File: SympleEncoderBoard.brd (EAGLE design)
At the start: 50.8 x 50.8 mm, 31 parts, among them IC1 STM32F446RET6

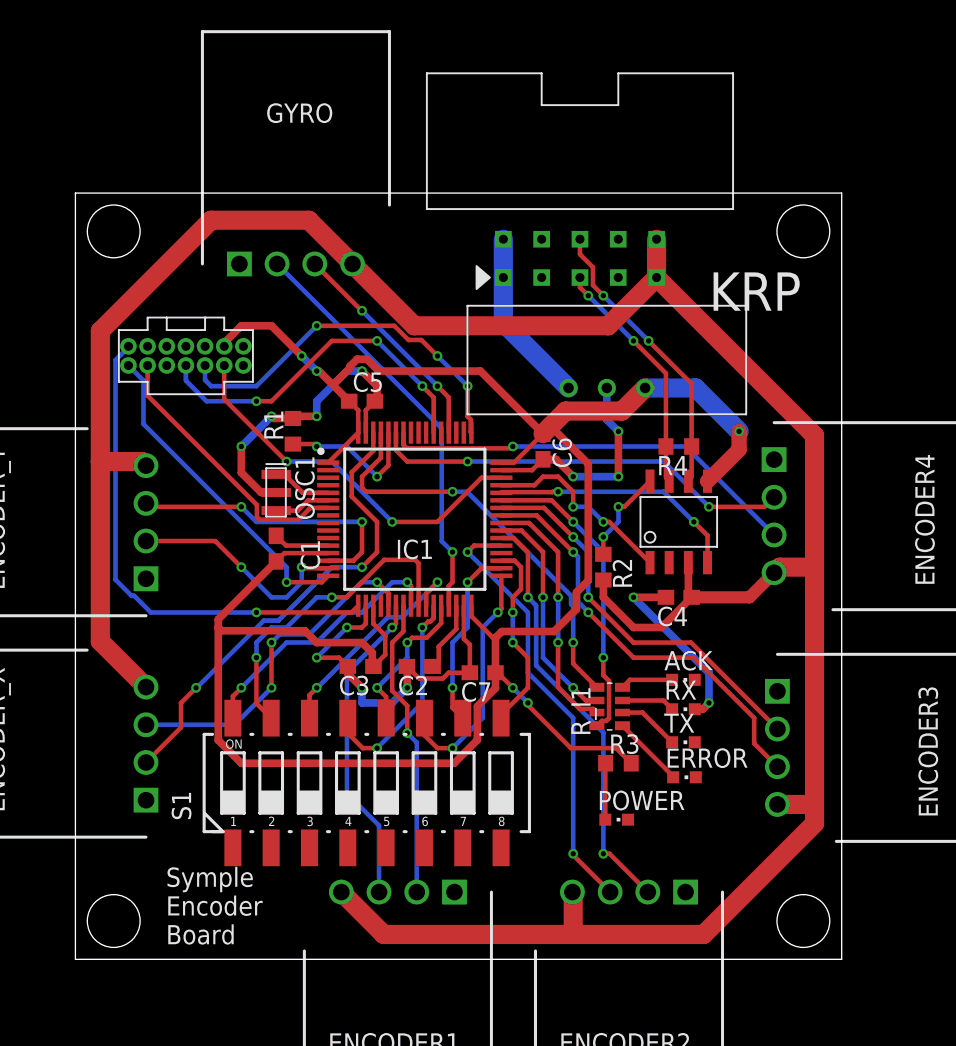
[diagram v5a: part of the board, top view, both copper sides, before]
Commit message: GYRO用XHコネクタを横から縦に、テキストの文字を少し拡大、ベタパターンDRCチェック済
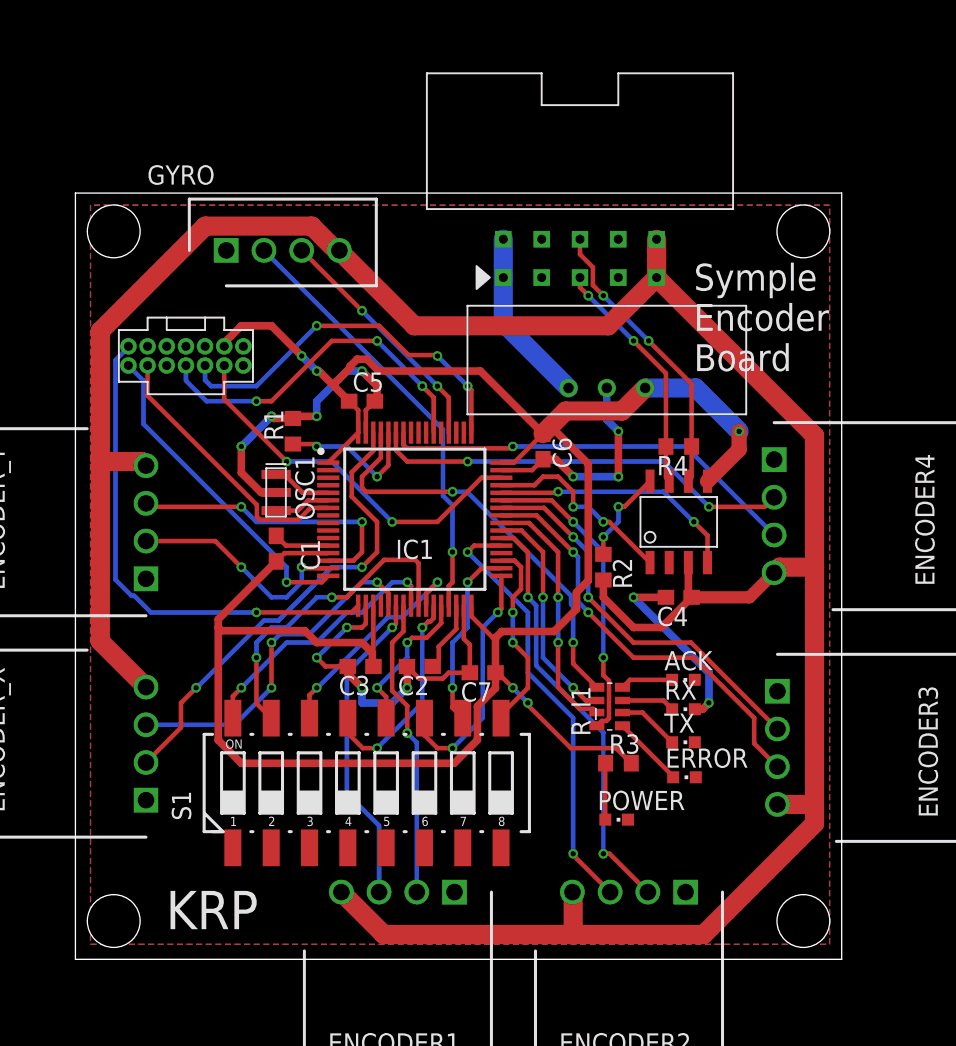
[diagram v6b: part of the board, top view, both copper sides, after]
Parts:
- GYRO: value S4B-XH-A_LF__SN_ -> B4B-XH-A_LF__SN_; device S4B-XH-A_LF__SN_:SHDRRA4W64P0X250_1X4_1240X1150 -> B4B-XH-A_LF__SN_:SHDR4W64P0X250_1X4_1240X575X70
- moved GYRO 1.25 mm to (10.0, 47.0)
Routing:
- net I2C_SCL: track 27.6 -> 28.8 mm
- net I2C_SDA: track 14.9 -> 16.1 mm
- net +3.3V: track 149.6 -> 149.0 mm
- added copper zone on layer 1, net GND
- added copper zone on layer 16, net GND

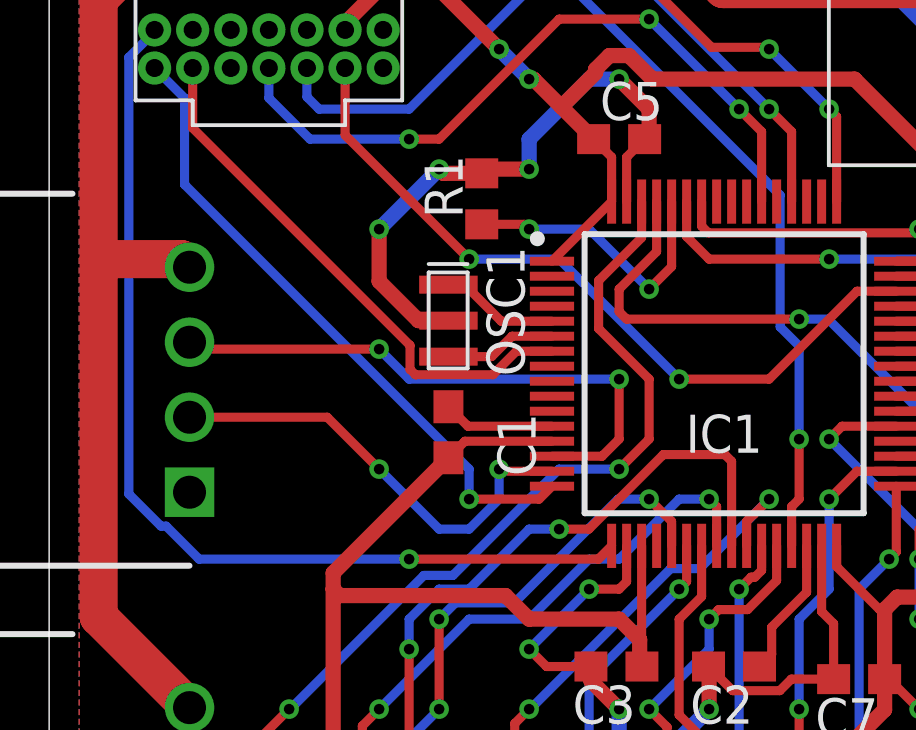
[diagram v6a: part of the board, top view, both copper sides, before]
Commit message: GRYO用コネクタを横から縦に、テキストの文字を少し拡大、ベタパターンDRCチェック済、ガーバーデータ追加
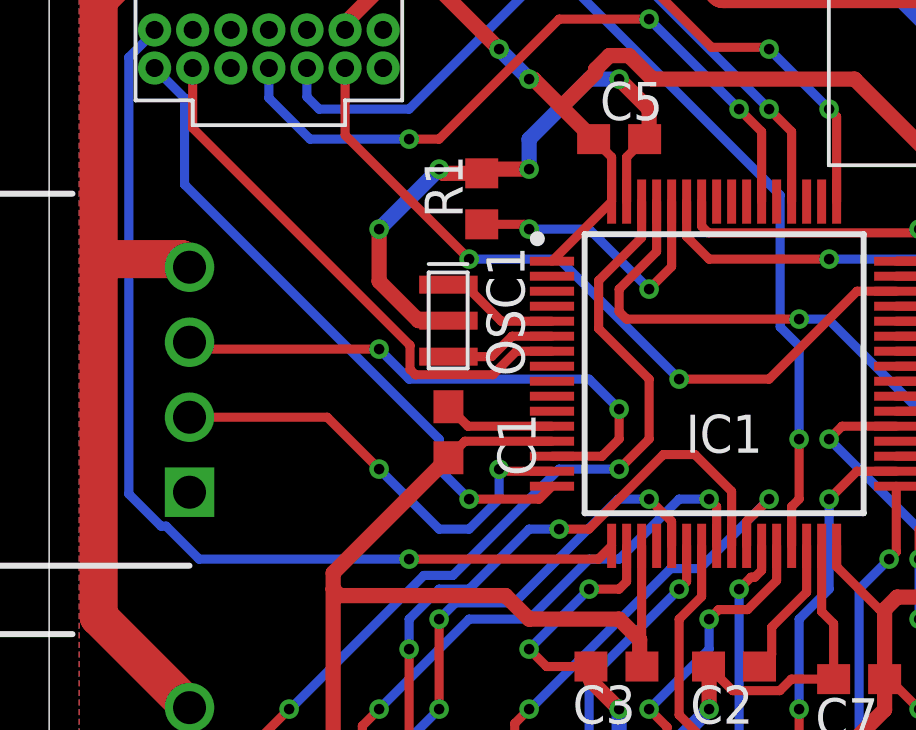
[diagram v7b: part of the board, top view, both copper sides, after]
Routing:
- net SW7: track 21.3 -> 20.8 mm
- net ENY_A: track 19.3 -> 18.7 mm
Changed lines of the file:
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@@
 <wire x1="16.332" y1="25" x2="14" y2="25" width="0.3048" layer="1"/>
 <via x="14" y="25" extent="1-16" drill="0.35"/>
-<wire x1="14" y1="25" x2="14" y2="26" width="0.3048" layer="16"/>
-<wire x1="14" y1="26" x2="4.515" y2="35.485" width="0.3048" layer="16"/>
+<wire x1="13" y1="27" x2="13" y2="26" width="0.3048" layer="16"/>
+<wire x1="14" y1="25" x2="13" y2="26" width="0.3048" layer="16"/>
+<wire x1="13" y1="27" x2="4.515" y2="35.485" width="0.3048" layer="16"/>
 <wire x1="4.515" y1="38.37" x2="4.515" y2="35.485" width="0.3048" layer="16"/>
 <wire x1="4.515" y1="38.37" x2="3.515" y2="39.37" width="0.3048" layer="16"/>
@@
 <contactref element="IC1" pad="14"/>
 <contactref element="ENCODER_Y" pad="3"/>
-<via x="19" y="29" extent="1-16" drill="0.35"/>
-<wire x1="19" y1="29" x2="12" y2="29" width="0.3048" layer="16"/>
+<via x="19" y="28" extent="1-16" drill="0.35"/>
+<wire x1="19" y1="28" x2="18" y2="29" width="0.3048" layer="16"/>
+<wire x1="18" y1="29" x2="12" y2="29" width="0.3048" layer="16"/>
 <wire x1="12" y1="29" x2="11" y2="30" width="0.3048" layer="16"/>
 <via x="11" y="30" extent="1-16" drill="0.35"/>
 <wire x1="11" y1="30" x2="4.91" y2="30" width="0.3048" layer="1"/>
 <wire x1="4.91" y1="30" x2="4.68" y2="30.23" width="0.3048" layer="1"/>
-<wire x1="19" y1="29" x2="19" y2="27" width="0.3048" layer="1"/>
+<wire x1="19" y1="28" x2="19" y2="27" width="0.3048" layer="1"/>
 <wire x1="19" y1="27" x2="18.43" y2="26.43" width="0.3048" layer="1"/>
 <wire x1="18.43" y1="26.43" x2="16.762" y2="26.43" width="0.3048" layer="1"/>
@@
 <wire x1="17" y1="24" x2="17.98945" y2="24" width="0.3048" layer="1"/>
 <wire x1="20.47375" y1="26.4843" x2="17.98945" y2="24" width="0.3048" layer="1"/>
-<wire x1="22.52625" y1="26.4843" x2="20.47375" y2="26.4843" width="0.3048" layer="1"/>
+<wire x1="21.52625" y1="26.4843" x2="20.47375" y2="26.4843" width="0.3048" layer="1"/>
 <wire x1="12.98" y1="15.99" x2="12" y2="16.97" width="0.3048" layer="1"/>
 <wire x1="12" y1="16.97" x2="12" y2="20" width="0.3048" layer="1"/>
@@
 <via x="12" y="20" extent="1-16" drill="0.35"/>
 <wire x1="17" y1="24" x2="16" y2="24" width="0.3048" layer="16"/>
-<wire x1="22.75" y1="23.442" x2="22.75" y2="26.26055" width="0.3048" layer="1"/>
-<wire x1="22.75" y1="26.26055" x2="22.52625" y2="26.4843" width="0.3048" layer="1"/>
+<wire x1="22.75" y1="23.442" x2="22.75" y2="25.26055" width="0.3048" layer="1"/>
+<wire x1="22.75" y1="25.26055" x2="21.52625" y2="26.4843" width="0.3048" layer="1"/>
 <wire x1="16" y1="24" x2="14" y2="22" width="0.3048" layer="16"/>
 <wire x1="14" y1="22" x2="13" y2="22" width="0.3048" layer="16"/>

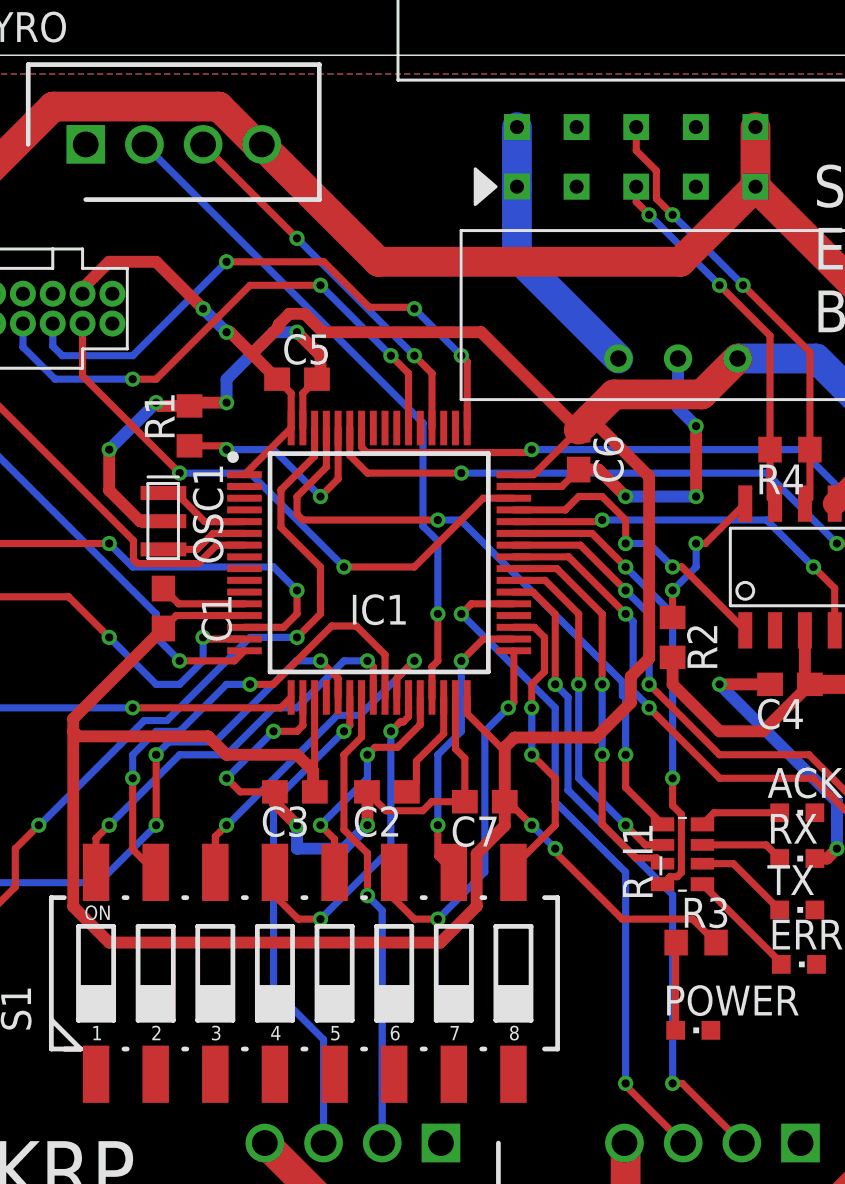
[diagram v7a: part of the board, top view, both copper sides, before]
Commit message: 配線を何箇所か短くした
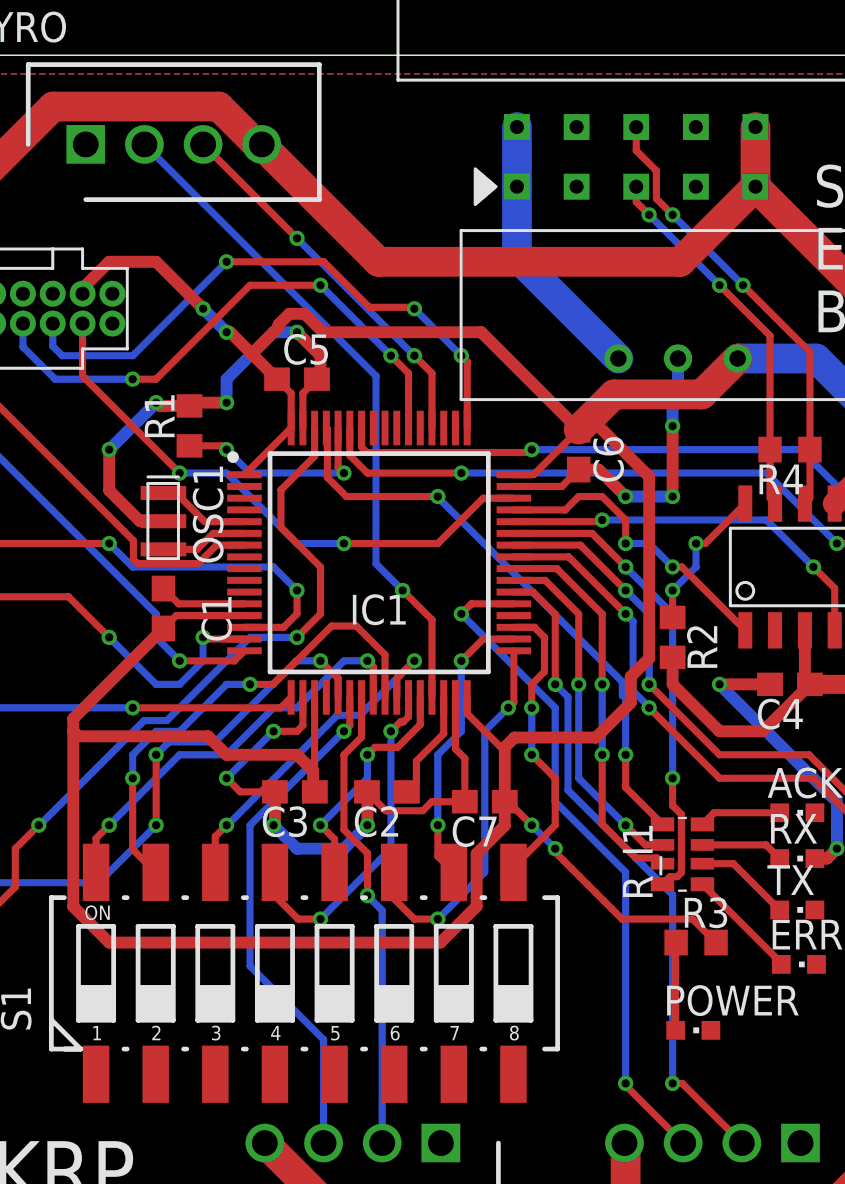
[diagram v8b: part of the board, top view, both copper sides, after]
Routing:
- net LEDGYRO: track 27.8 -> 25.1 mm
- net GND: track 75.6 -> 74.4 mm
- net SWDIO: track 25.2 -> 24.4 mm
- net EN1_A: track 21.2 -> 22.0 mm
- net N$1: track 9.70 -> 9.08 mm
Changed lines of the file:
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@@
 <wire x1="26.15" y1="20.85" x2="26.15" y2="19" width="0.3048" layer="1"/>
 <wire x1="25.75" y1="21.25" x2="26.15" y2="20.85" width="0.3048" layer="1"/>
-<wire x1="18.06" y1="19.42" x2="18.06" y2="18.94" width="0.508" layer="1"/>
-<wire x1="18.06" y1="18.94" x2="19" y2="18" width="0.508" layer="1"/>
+<wire x1="18.06" y1="19.42" x2="18.06" y2="18.06" width="0.508" layer="1"/>
+<wire x1="18.06" y1="18.06" x2="18" y2="18" width="0.508" layer="1"/>
 <wire x1="21.98" y1="19.42" x2="22" y2="19.4" width="0.508" layer="1"/>
 <wire x1="22" y1="19.4" x2="22" y2="18" width="0.508" layer="1"/>
-<via x="19" y="18" extent="1-16" drill="0.35"/>
+<via x="18" y="18" extent="1-16" drill="0.35"/>
 <via x="22" y="18" extent="1-16" drill="0.35"/>
-<wire x1="19" y1="18" x2="19" y2="17" width="0.508" layer="16"/>
+<wire x1="18" y1="18" x2="19" y2="17" width="0.508" layer="16"/>
 <wire x1="21" y1="17" x2="19" y2="17" width="0.508" layer="16"/>
 <wire x1="21" y1="17" x2="22" y2="18" width="0.508" layer="16"/>
@@
 <wire x1="31.85" y1="33.15" x2="33" y2="32" width="0.508" layer="1"/>
 <via x="33" y="32" extent="1-16" drill="0.35"/>
-<wire x1="33" y1="32" x2="36" y2="32" width="0.508" layer="16"/>
-<wire x1="35.23" y1="37.88" x2="35.23" y2="35.77" width="0.508" layer="16"/>
-<wire x1="35.23" y1="35.77" x2="36" y2="35" width="0.508" layer="16"/>
-<via x="36" y="35" extent="1-16" drill="0.35"/>
-<via x="36" y="32" extent="1-16" drill="0.35"/>
-<wire x1="36" y1="35" x2="36" y2="32" width="0.508" layer="1"/>
+<wire x1="33" y1="32" x2="35" y2="32" width="0.508" layer="16"/>
+<wire x1="35.23" y1="37.88" x2="35.23" y2="36.23" width="0.508" layer="16"/>
+<wire x1="35.23" y1="36.23" x2="35" y2="36" width="0.508" layer="16"/>
+<wire x1="35" y1="36" x2="35" y2="35" width="0.508" layer="16"/>
+<via x="35" y="35" extent="1-16" drill="0.35"/>
+<via x="35" y="32" extent="1-16" drill="0.35"/>
+<wire x1="35" y1="35" x2="35" y2="32" width="0.508" layer="1"/>
 <wire x1="24.74105" y1="19" x2="26.15" y2="19" width="0.3048" layer="1"/>
 <wire x1="24.35625" y1="18.6152" x2="24.74105" y2="19" width="0.3048" layer="1"/>
@@
 <wire x1="34.57" y1="18.035" x2="33" y2="19.605" width="0.3048" layer="1"/>
 <wire x1="33" y1="19.605" x2="33" y2="21" width="0.3048" layer="1"/>
-<wire x1="20.25" y1="34.918" x2="20.25" y2="33.25" width="0.3048" layer="1"/>
-<wire x1="20.25" y1="33.25" x2="19" y2="32" width="0.3048" layer="1"/>
-<wire x1="19" y1="32" x2="19" y2="31.25" width="0.3048" layer="1"/>
-<wire x1="19" y1="31.25" x2="19.25" y2="31" width="0.3048" layer="1"/>
-<wire x1="25" y1="31" x2="25.9659125" y2="31" width="0.3048" layer="16"/>
-<via x="25" y="31" extent="1-16" drill="0.35"/>
-<wire x1="19.25" y1="31" x2="25" y2="31" width="0.3048" layer="1"/>
+<wire x1="25" y1="32" x2="24.98295625" y2="31.98295625" width="0.3048" layer="16"/>
+<via x="25" y="32" extent="1-16" drill="0.35"/>
 <wire x1="32.8598" y1="24.1061125" x2="32.8598" y2="23.52770625" width="0.3048" layer="16"/>
 <wire x1="32.8598" y1="23.52770625" x2="33" y2="23.38750625" width="0.3048" layer="16"/>
 <wire x1="33" y1="23.38750625" x2="33" y2="21" width="0.3048" layer="16"/>
-<wire x1="25.9659125" y1="31" x2="32.8598" y2="24.1061125" width="0.3048" layer="16"/>
+<wire x1="24.98295625" y1="31.98295625" x2="32.8598" y2="24.1061125" width="0.3048" layer="16"/>
+<wire x1="20.25" y1="34.918" x2="20.2928" y2="34.8752" width="0.3048" layer="1"/>
+<wire x1="20.2928" y1="34.8752" x2="20.2928" y2="32.81313125" width="0.3048" layer="1"/>
+<wire x1="20.2928" y1="32.81313125" x2="21.10593125" y2="32" width="0.3048" layer="1"/>
+<wire x1="21.10593125" y1="32" x2="25" y2="32" width="0.3048" layer="1"/>
 </signal>
 <signal name="N$1">
 <contactref element="R1" pad="1"/>
 <contactref element="IC1" pad="60"/>
-<wire x1="20.75" y1="34.918" x2="20.75" y2="32.75" width="0.3048" layer="1"/>
-<wire x1="20.75" y1="32.75" x2="20" y2="32" width="0.3048" layer="1"/>
+<wire x1="20.75" y1="34.918" x2="20.75" y2="33.249996875" width="0.3048" layer="1"/>
+<wire x1="20.75" y1="33.249996875" x2="21" y2="33" width="0.3048" layer="1"/>
 <via x="16" y="34" extent="1-16" drill="0.35"/>
-<via x="20" y="32" extent="1-16" drill="0.35"/>
-<wire x1="20" y1="32" x2="18" y2="34" width="0.3048" layer="16"/>
-<wire x1="18" y1="34" x2="16" y2="34" width="0.3048" layer="16"/>
+<via x="21" y="33" extent="1-16" drill="0.35"/>
+<wire x1="21" y1="33" x2="17" y2="33" width="0.3048" layer="16"/>
+<wire x1="17" y1="33" x2="16" y2="34" width="0.3048" layer="16"/>
 <wire x1="14.42" y1="34.16" x2="15.84" y2="34.16" width="0.3048" layer="1"/>
 <wire x1="15.84" y1="34.16" x2="16" y2="34" width="0.3048" layer="1"/>
@@
 <contactref element="IC1" pad="46"/>
 <contactref element="U$1" pad="4"/>
-<via x="21" y="29" extent="1-16" drill="0.35"/>
+<via x="21" y="30" extent="1-16" drill="0.35"/>
 <via x="14" y="33" extent="1-16" drill="0.35"/>
-<wire x1="14" y1="33" x2="17" y2="33" width="0.3048" layer="16"/>
-<wire x1="21" y1="29" x2="17" y2="33" width="0.3048" layer="16"/>
+<wire x1="14" y1="33" x2="16" y2="33" width="0.3048" layer="16"/>
+<wire x1="21" y1="30" x2="19" y2="30" width="0.3048" layer="16"/>
+<wire x1="19" y1="30" x2="16" y2="33" width="0.3048" layer="16"/>
 <wire x1="14" y1="33" x2="9.865" y2="37.135" width="0.3048" layer="1"/>
 <wire x1="9.865" y1="37.135" x2="9.865" y2="39.37" width="0.3048" layer="1"/>
-<wire x1="26.93" y1="31.93" x2="24" y2="29" width="0.3048" layer="1"/>
-<wire x1="21" y1="29" x2="24" y2="29" width="0.3048" layer="1"/>
+<wire x1="26.93" y1="31.93" x2="25" y2="30" width="0.3048" layer="1"/>
+<wire x1="25" y1="30" x2="21" y2="30" width="0.3048" layer="1"/>
 <wire x1="28.238" y1="31.93" x2="26.93" y2="31.93" width="0.3048" layer="1"/>
 </signal>
@@
 <signal name="I2C_SCL">
 <contactref element="IC1" pad="29"/>
-<wire x1="24.75" y1="23.442" x2="24.75" y2="24.75" width="0.3048" layer="1"/>
-<wire x1="24.75" y1="24.75" x2="25" y2="25" width="0.3048" layer="1"/>
-<wire x1="25" y1="25" x2="25" y2="27" width="0.3048" layer="1"/>
-<via x="25" y="27" extent="1-16" drill="0.35"/>
+<wire x1="24.75" y1="26.75" x2="24.75" y2="23.442" width="0.3048" layer="1"/>
+<wire x1="24.75" y1="26.75" x2="23.5" y2="28" width="0.3048" layer="1"/>
+<via x="23.5" y="28" extent="1-16" drill="0.35"/>
 <contactref element="GYRO" pad="2"/>
-<wire x1="25" y1="30.10593125" x2="25" y2="27" width="0.3048" layer="16"/>
-<wire x1="24.3678" y1="30.73813125" x2="25" y2="30.10593125" width="0.3048" layer="16"/>
-<wire x1="12.5" y1="47" x2="24.3678" y2="35.1322" width="0.3048" layer="16"/>
-<wire x1="24.3678" y1="35.1322" x2="24.3678" y2="30.73813125" width="0.3048" layer="16"/>
+<wire x1="12.5" y1="47" x2="22.3678" y2="37.1322" width="0.3048" layer="16"/>
+<wire x1="22.3678" y1="29.1322" x2="23.5" y2="28" width="0.3048" layer="16"/>
+<wire x1="22.3678" y1="37.1322" x2="22.3678" y2="29.1322" width="0.3048" layer="16"/>
 </signal>
 <signal name="SW4">
@@
 <wire x1="21.25" y1="22.25" x2="21" y2="22" width="0.3048" layer="1"/>
 <via x="21" y="22" extent="1-16" drill="0.35"/>
-<wire x1="21" y1="22" x2="18" y2="19" width="0.3048" layer="16"/>
-<wire x1="18" y1="19" x2="18" y2="11" width="0.3048" layer="16"/>
+<wire x1="21" y1="22" x2="17" y2="18" width="0.3048" layer="16"/>
+<wire x1="17" y1="18" x2="17" y2="12" width="0.3048" layer="16"/>
 <wire x1="20.13" y1="8.87" x2="20.13" y2="4.46" width="0.3048" layer="16"/>
-<wire x1="18" y1="11" x2="20.13" y2="8.87" width="0.3048" layer="16"/>
+<wire x1="17" y1="12" x2="20.13" y2="8.87" width="0.3048" layer="16"/>
 </signal>
 <signal name="SW6">
